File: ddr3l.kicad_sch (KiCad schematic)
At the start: 35 parts, among them U4 MCIMX6Y2DVM09AB, U6 IS43TR16256BL-107MBL

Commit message: Update symbols
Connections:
- net VDD renamed VDD_1V35

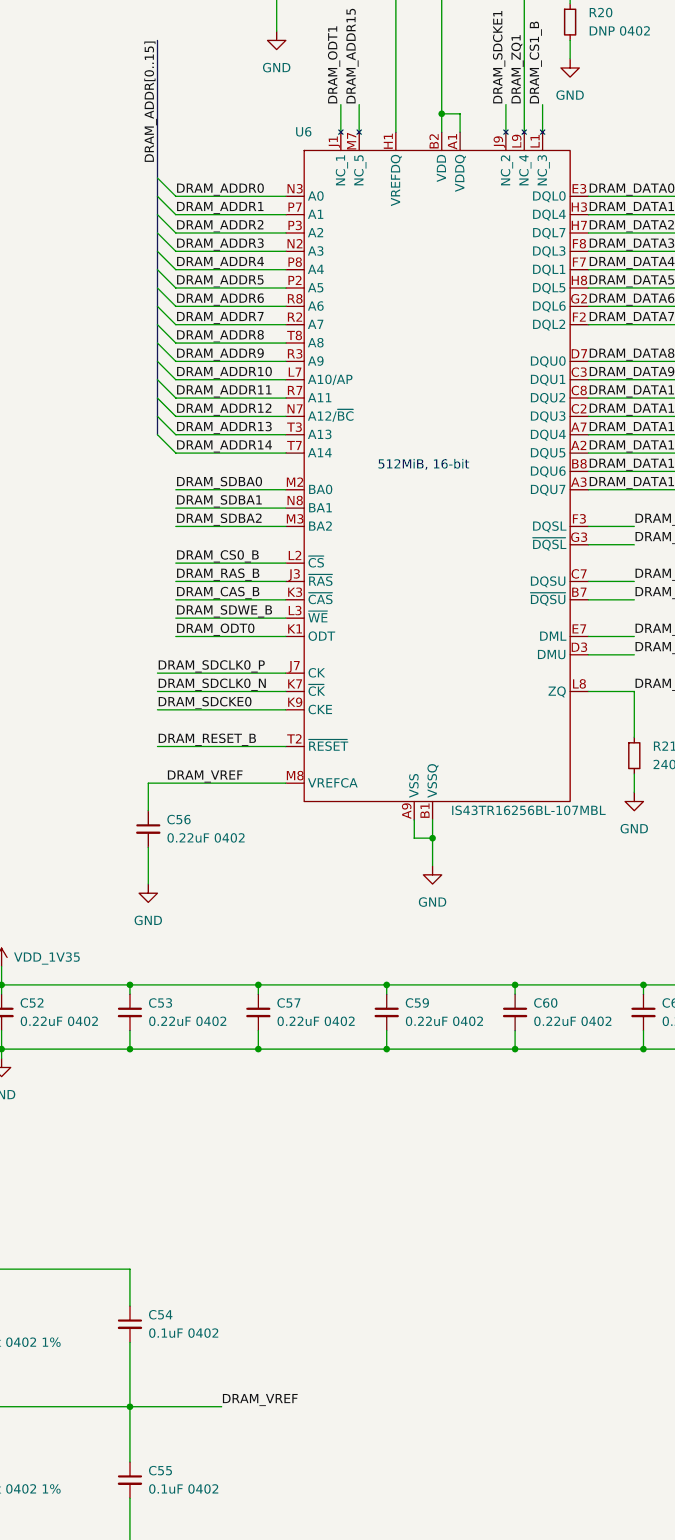
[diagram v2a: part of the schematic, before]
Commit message: Change DDR NC electrical type to Passive so they can be connected
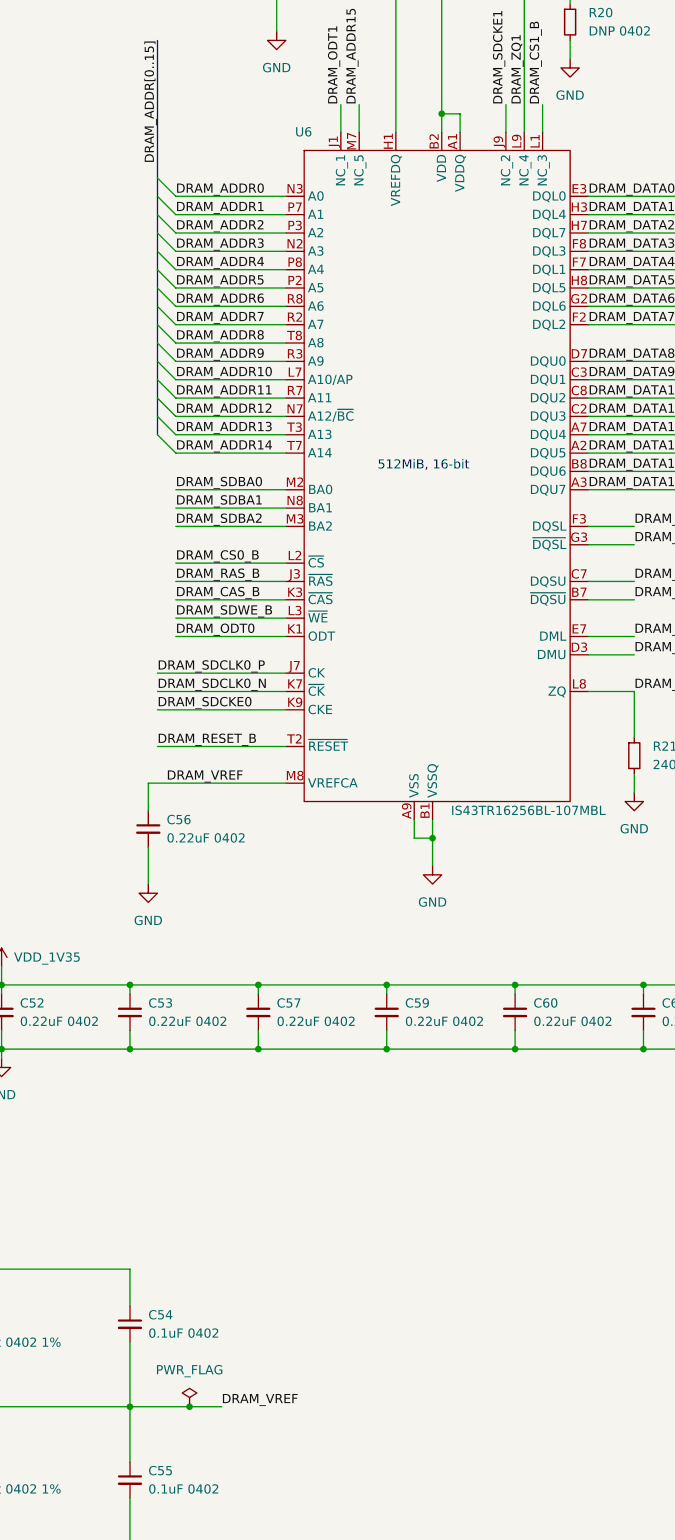
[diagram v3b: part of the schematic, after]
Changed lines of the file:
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@@
   (junction (at 77.47 139.7) (diameter 0) (color 0 0 0 0)
   )
+  (junction (at 245.745 223.52) (diameter 0) (color 0 0 0 0)
+  )
   (junction (at 308.61 173.99) (diameter 0) (color 0 0 0 0)
   )
@@
     (stroke (width 0) (type default) (color 0 0 0 0))
   )
-  (wire (pts (xy 237.49 223.52) (xy 250.19 223.52))
+  (wire (pts (xy 237.49 223.52) (xy 245.745 223.52))
     (stroke (width 0) (type default) (color 0 0 0 0))
   )
@@
   )
   (wire (pts (xy 213.36 215.9) (xy 213.36 223.52))
+    (stroke (width 0) (type default) (color 0 0 0 0))
+  )
+  (wire (pts (xy 245.745 223.52) (xy 250.19 223.52))
     (stroke (width 0) (type default) (color 0 0 0 0))
   )
@@
       (effects (font (size 1.27 1.27)) hide)
     )
+    (pin "1")
+  )
+  (symbol (lib_id "power:PWR_FLAG") (at 245.745 223.52 0) (unit 1)
+    (in_bom yes) (on_board yes) (fields_autoplaced)
+    (property "Reference" "#FLG0103" (id 0) (at 245.745 221.615 0)
+      (effects (font (size 1.27 1.27)) hide)
+    )
+    (property "Value" "PWR_FLAG" (id 1) (at 245.745 218.44 0))
+    (property "Footprint" "" (id 2) (at 245.745 223.52 0)
+      (effects (font (size 1.27 1.27)) hide)
+    )
+    (property "Datasheet" "~" (id 3) (at 245.745 223.52 0)
+      (effects (font (size 1.27 1.27)) hide)
+    )

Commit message: Footprint assignments for standard passives
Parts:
- C43, C44, C45, C46, C47, C49, C50, C52, C53, C54, C55, C56, C57, C58, C59, C60, C61, C62, C63, C64, C65, C66: footprint (none) -> Capacitor_SMD:C_0402_1005Metric
- C48: footprint (none) -> Capacitor_SMD:C_0805_2012Metric
- C51: footprint (none) -> Capacitor_SMD:C_0603_1608Metric
- R13, R14, R15, R16, R17, R18, R19, R20, R21: footprint (none) -> Resistor_SMD:R_0402_1005Metric
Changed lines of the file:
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@@
       (effects (font (size 1.27 1.27)) (justify left))
     )
-    (property "Footprint" "" (id 2) (at 219.71 168.91 0)
+    (property "Footprint" "Capacitor_SMD:C_0402_1005Metric" (id 2) (at 219.71 168.91 0)
       (effects (font (size 1.27 1.27)) hide)
     )
@@
       (effects (font (size 1.27 1.27)) (justify left))
     )
-    (property "Footprint" "" (id 2) (at 397.51 168.91 0)
+    (property "Footprint" "Capacitor_SMD:C_0402_1005Metric" (id 2) (at 397.51 168.91 0)
       (effects (font (size 1.27 1.27)) hide)
     )
@@
       (effects (font (size 1.27 1.27)) (justify left))
     )
-    (property "Footprint" "" (id 2) (at 179.07 128.27 0)
+    (property "Footprint" "Resistor_SMD:R_0402_1005Metric" (id 2) (at 179.07 128.27 0)
       (effects (font (size 1.27 1.27)) hide)
     )
@@
       (effects (font (size 1.27 1.27)) (justify left))
     )
-    (property "Footprint" "" (id 2) (at 240.03 143.51 0)
+    (property "Footprint" "Capacitor_SMD:C_0402_1005Metric" (id 2) (at 240.03 143.51 0)
       (effects (font (size 1.27 1.27)) hide)
     )
@@
       (effects (font (size 1.27 1.27)) (justify left))
     )
-    (property "Footprint" "" (id 2) (at 194.31 223.52 0)
+    (property "Footprint" "Capacitor_SMD:C_0603_1608Metric" (id 2) (at 194.31 223.52 0)
       (effects (font (size 1.27 1.27)) hide)
     )
@@
       (effects (font (size 1.27 1.27)) (justify left))
     )
-    (property "Footprint" "" (id 2) (at 168.91 199.39 0)
+    (property "Footprint" "Resistor_SMD:R_0402_1005Metric" (id 2) (at 168.91 199.39 0)
       (effects (font (size 1.27 1.27)) hide)
     )
@@
       (effects (font (size 1.27 1.27)) (justify left))
     )
-    (property "Footprint" "" (id 2) (at 101.6 168.91 0)
+    (property "Footprint" "Capacitor_SMD:C_0402_1005Metric" (id 2) (at 101.6 168.91 0)
       (effects (font (size 1.27 1.27)) hide)
     )
@@
       (effects (font (size 1.27 1.27)) (justify left))
     )
-    (property "Footprint" "" (id 2) (at 168.91 247.65 0)
+    (property "Footprint" "Capacitor_SMD:C_0402_1005Metric" (id 2) (at 168.91 247.65 0)
       (effects (font (size 1.27 1.27)) hide)
     )
@@
       (effects (font (size 1.27 1.27)) (justify left))
     )
-    (property "Footprint" "" (id 2) (at 379.73 168.91 0)
+    (property "Footprint" "Capacitor_SMD:C_0402_1005Metric" (id 2) (at 379.73 168.91 0)
       (effects (font (size 1.27 1.27)) hide)
     )
@@
       (effects (font (size 1.27 1.27)) (justify left))
     )
-    (property "Footprint" "" (id 2) (at 257.81 25.4 0)
+    (property "Footprint" "Capacitor_SMD:C_0402_1005Metric" (id 2) (at 257.81 25.4 0)
       (effects (font (size 1.27 1.27)) hide)
     )
@@
       (effects (font (size 1.27 1.27)) (justify left))
     )
-    (property "Footprint" "" (id 2) (at 361.95 168.91 0)
+    (property "Footprint" "Capacitor_SMD:C_0402_1005Metric" (id 2) (at 361.95 168.91 0)
       (effects (font (size 1.27 1.27)) hide)
     )
@@
       (effects (font (size 1.27 1.27)) (justify left))
     )
-    (property "Footprint" "" (id 2) (at 213.36 233.68 0)
+    (property "Footprint" "Resistor_SMD:R_0402_1005Metric" (id 2) (at 213.36 233.68 0)
       (effects (font (size 1.27 1.27)) hide)
     )
@@
       (effects (font (size 1.27 1.27)) (justify left))
     )
-    (property "Footprint" "" (id 2) (at 137.16 168.91 0)
+    (property "Footprint" "Capacitor_SMD:C_0402_1005Metric" (id 2) (at 137.16 168.91 0)
       (effects (font (size 1.27 1.27)) hide)
     )
@@
     (property "Reference" "R13" (id 0) (at 50.8 138.43 0))
     (property "Value" "10k 0402" (id 1) (at 54.61 140.97 0))
-    (property "Footprint" "" (id 2) (at 48.26 139.7 0)
+    (property "Footprint" "Resistor_SMD:R_0402_1005Metric" (id 2) (at 48.26 139.7 0)
       (effects (font (size 1.27 1.27)) hide)
     )
@@
       (effects (font (size 1.27 1.27)) (justify left))
     )
-    (property "Footprint" "" (id 2) (at 165.1 128.27 0)
+    (property "Footprint" "Resistor_SMD:R_0402_1005Metric" (id 2) (at 165.1 128.27 0)
       (effects (font (size 1.27 1.27)) hide)
     )
@@
       (effects (font (size 1.27 1.27)) (justify left))
     )
-    (property "Footprint" "" (id 2) (at 326.39 168.91 0)
+    (property "Footprint" "Capacitor_SMD:C_0402_1005Metric" (id 2) (at 326.39 168.91 0)
       (effects (font (size 1.27 1.27)) hide)
     )
@@
       (effects (font (size 1.27 1.27)) (justify left))
     )
-    (property "Footprint" "" (id 2) (at 95.25 144.78 0)
+    (property "Footprint" "Capacitor_SMD:C_0402_1005Metric" (id 2) (at 95.25 144.78 0)
       (effects (font (size 1.27 1.27)) hide)
     )
@@
       (effects (font (size 1.27 1.27)) (justify left))
     )
-    (property "Footprint" "" (id 2) (at 290.83 168.91 0)
+    (property "Footprint" "Capacitor_SMD:C_0402_1005Metric" (id 2) (at 290.83 168.91 0)
       (effects (font (size 1.27 1.27)) hide)
     )
@@
       (effects (font (size 1.27 1.27)) (justify left))
     )
-    (property "Footprint" "" (id 2) (at 255.27 168.91 0)
+    (property "Footprint" "Capacitor_SMD:C_0402_1005Metric" (id 2) (at 255.27 168.91 0)
       (effects (font (size 1.27 1.27)) hide)
     )
@@
       (effects (font (size 1.27 1.27)) (justify left))
     )
-    (property "Footprint" "" (id 2) (at 168.91 223.52 0)
+    (property "Footprint" "Capacitor_SMD:C_0402_1005Metric" (id 2) (at 168.91 223.52 0)
       (effects (font (size 1.27 1.27)) hide)
     )
@@
       (effects (font (size 1.27 1.27)) (justify left))
     )
-    (property "Footprint" "" (id 2) (at 237.49 233.68 0)
+    (property "Footprint" "Capacitor_SMD:C_0402_1005Metric" (id 2) (at 237.49 233.68 0)
       (effects (font (size 1.27 1.27)) hide)
     )
@@
       (effects (font (size 1.27 1.27)) (justify left))
     )
-    (property "Footprint" "" (id 2) (at 213.36 213.36 0)
+    (property "Footprint" "Resistor_SMD:R_0402_1005Metric" (id 2) (at 213.36 213.36 0)
       (effects (font (size 1.27 1.27)) hide)
     )
@@
       (effects (font (size 1.27 1.27)) (justify left))
     )
-    (property "Footprint" "" (id 2) (at 344.17 168.91 0)
+    (property "Footprint" "Capacitor_SMD:C_0402_1005Metric" (id 2) (at 344.17 168.91 0)
       (effects (font (size 1.27 1.27)) hide)
     )
@@
       (effects (font (size 1.27 1.27)) (justify left))
     )
-    (property "Footprint" "" (id 2) (at 119.38 168.91 0)
+    (property "Footprint" "Capacitor_SMD:C_0402_1005Metric" (id 2) (at 119.38 168.91 0)
       (effects (font (size 1.27 1.27)) hide)
     )
@@
       (effects (font (size 1.27 1.27)) (justify left))
     )
-    (property "Footprint" "" (id 2) (at 77.47 144.78 0)
+    (property "Footprint" "Capacitor_SMD:C_0402_1005Metric" (id 2) (at 77.47 144.78 0)
       (effects (font (size 1.27 1.27)) hide)
     )
@@
       (effects (font (size 1.27 1.27)) (justify left))
     )
-    (property "Footprint" "" (id 2) (at 237.49 168.91 0)
+    (property "Footprint" "Capacitor_SMD:C_0402_1005Metric" (id 2) (at 237.49 168.91 0)
       (effects (font (size 1.27 1.27)) hide)
     )
@@
       (effects (font (size 1.27 1.27)) (justify left))
     )
-    (property "Footprint" "" (id 2) (at 273.05 168.91 0)
+    (property "Footprint" "Capacitor_SMD:C_0402_1005Metric" (id 2) (at 273.05 168.91 0)
       (effects (font (size 1.27 1.27)) hide)
     )
@@
       (effects (font (size 1.27 1.27)) (justify left))
     )
-    (property "Footprint" "" (id 2) (at 237.49 212.09 0)
+    (property "Footprint" "Capacitor_SMD:C_0402_1005Metric" (id 2) (at 237.49 212.09 0)
       (effects (font (size 1.27 1.27)) hide)
     )
@@
       (effects (font (size 1.27 1.27)) (justify right))
     )
-    (property "Footprint" "" (id 2) (at 60.96 139.7 0)
+    (property "Footprint" "Resistor_SMD:R_0402_1005Metric" (id 2) (at 60.96 139.7 0)
       (effects (font (size 1.27 1.27)) hide)
     )
@@
       (effects (font (size 1.27 1.27)) (justify left))
     )
-    (property "Footprint" "" (id 2) (at 298.45 31.75 0)
+    (property "Footprint" "Resistor_SMD:R_0402_1005Metric" (id 2) (at 298.45 31.75 0)
       (effects (font (size 1.27 1.27)) hide)
     )
@@
       (effects (font (size 1.27 1.27)) (justify left))
     )
-    (property "Footprint" "" (id 2) (at 154.94 168.91 0)
+    (property "Footprint" "Capacitor_SMD:C_0805_2012Metric" (id 2) (at 154.94 168.91 0)
       (effects (font (size 1.27 1.27)) hide)
     )
@@
       (effects (font (size 1.27 1.27)) (justify left))
     )
-    (property "Footprint" "" (id 2) (at 308.61 168.91 0)
+    (property "Footprint" "Capacitor_SMD:C_0402_1005Metric" (id 2) (at 308.61 168.91 0)
       (effects (font (size 1.27 1.27)) hide)
     )
@@
       (effects (font (size 1.27 1.27)) (justify left))
     )
-    (property "Footprint" "" (id 2) (at 307.34 133.35 0)
-      (effects (font (size 1.27 1.27)) hide)
-    )
+    (property "Footprint" "Resistor_SMD:R_0402_1005Metric" (id 2) (at 307.34 133.35 0)
+      (effects (font (size 1.27 1.27)) hide)
+    )
